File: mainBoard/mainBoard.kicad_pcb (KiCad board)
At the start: 4 copper layers, 132 x 85 mm, 78 parts, among them IC1 TCAN3414DR, J1 XT60PW-M, J10 RJ45, J11 RJ45, J12 Conn_01x03, J13 RJ45, J14 RJ45, J15 RJ45, J16 BM04B-SRSS-TB, J17 BM04B-SRSS-TB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

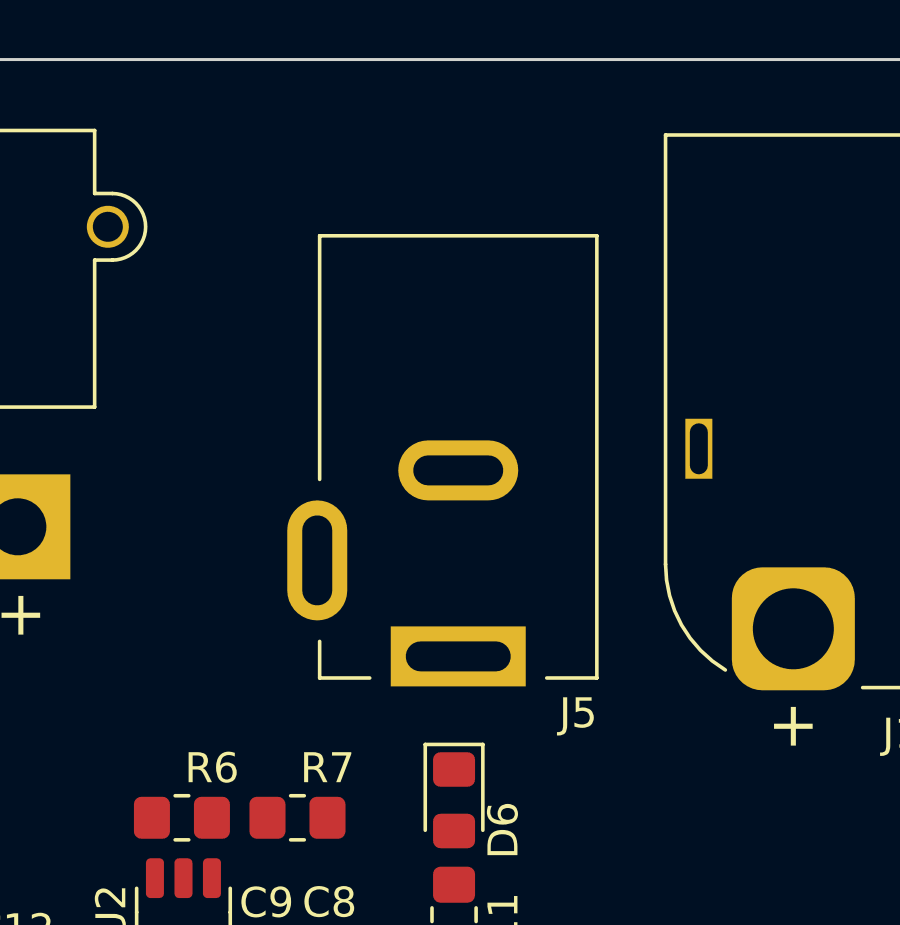
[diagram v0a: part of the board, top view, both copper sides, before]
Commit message: Moved barrel jack forward a bit
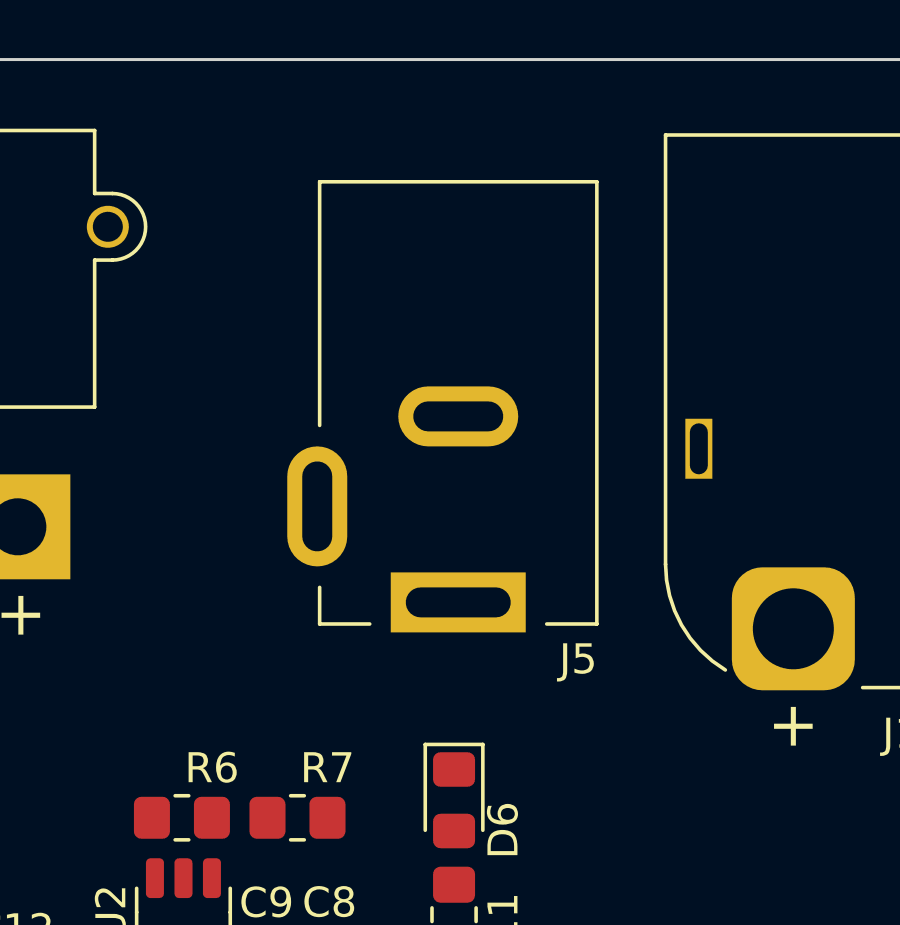
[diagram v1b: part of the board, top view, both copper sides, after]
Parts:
- moved J5 1.80 mm to (72.9, 30.1)
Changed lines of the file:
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@@
 	(footprint "Connector_BarrelJack:BarrelJack_Kycon_KLDX-0202-xC_Horizontal"
 		(layer "F.Cu")
-		(at 72.875 31.895 -90)
+		(at 72.875 30.095 -90)
 		(descr "DC Barrel Jack 2mm or 2.5mm center pin, https://www.kycon.com/Pub_Eng_Draw/KLDX-0202-AC%20&%20BC.pdf")
 		(tags "power jack 2mm 2.5mm KLDX-0202-BC KLDX-0202-AC")

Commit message: layed out mainboard as tano reccomended, added mounting holes, images, and new step file
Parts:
- removed D4, D5: 1SMA5925BT3G, Diode_SMD:D_SMA_Handsoldering
- removed D6, D7: LED, Diode_SMD:D_0805_2012Metric_Pad1.15x1.40mm_HandSolder
- removed R11, R12: 500, Resistor_SMD:R_0805_2012Metric_Pad1.20x1.40mm_HandSolder
- added H1: M4, MountingHole:MountingHole_4.3mm_M4_DIN965, F.Cu at (162.0, 19.0)
- added H2: M4, MountingHole:MountingHole_4.3mm_M4_DIN965, F.Cu at (264.0, 19.0)
- added H3: M4, MountingHole:MountingHole_4.3mm_M4_DIN965, F.Cu at (162.0, 86.0)
- added H4: M4, MountingHole:MountingHole_4.3mm_M4_DIN965, F.Cu at (264.0, 86.0)
- C10, C11, C12, C13, C8, C9, L2, Q2, R10, R14, R6, R7, U2: moved to B.Cu
- moved D3 211.1 mm to (258.3, 19.3), turned to 90 degrees
- moved R8 209.1 mm to (256.2, 19.3)
- moved J4 177.5 mm to (235.7, 28.6)
- moved C13 173.0 mm to (231.8, 41.0), turned to 180 degrees
- moved C12 173.0 mm to (231.8, 43.0), turned to 180 degrees
- moved L2 169.1 mm to (229.8, 47.6), turned to 0 degrees
- moved C11 165.0 mm to (227.7, 43.0), turned to 180 degrees
- moved R6 163.0 mm to (226.7, 36.7), turned to 0 degrees
- moved U2 162.9 mm to (226.6, 39.8)
- moved C9 157.3 mm to (223.8, 42.0)
- moved R7 155.3 mm to (222.8, 36.7), turned to 0 degrees
- moved C8 153.1 mm to (221.7, 42.0)
- moved C10 148.9 mm to (219.6, 42.0)
- moved Q2 144.7 mm to (214.8, 46.0), turned to -90 degrees
- moved R10 142.4 mm to (210.2, 48.3), turned to -90 degrees
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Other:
- board size 132 x 85 mm -> 110 x 75 mm

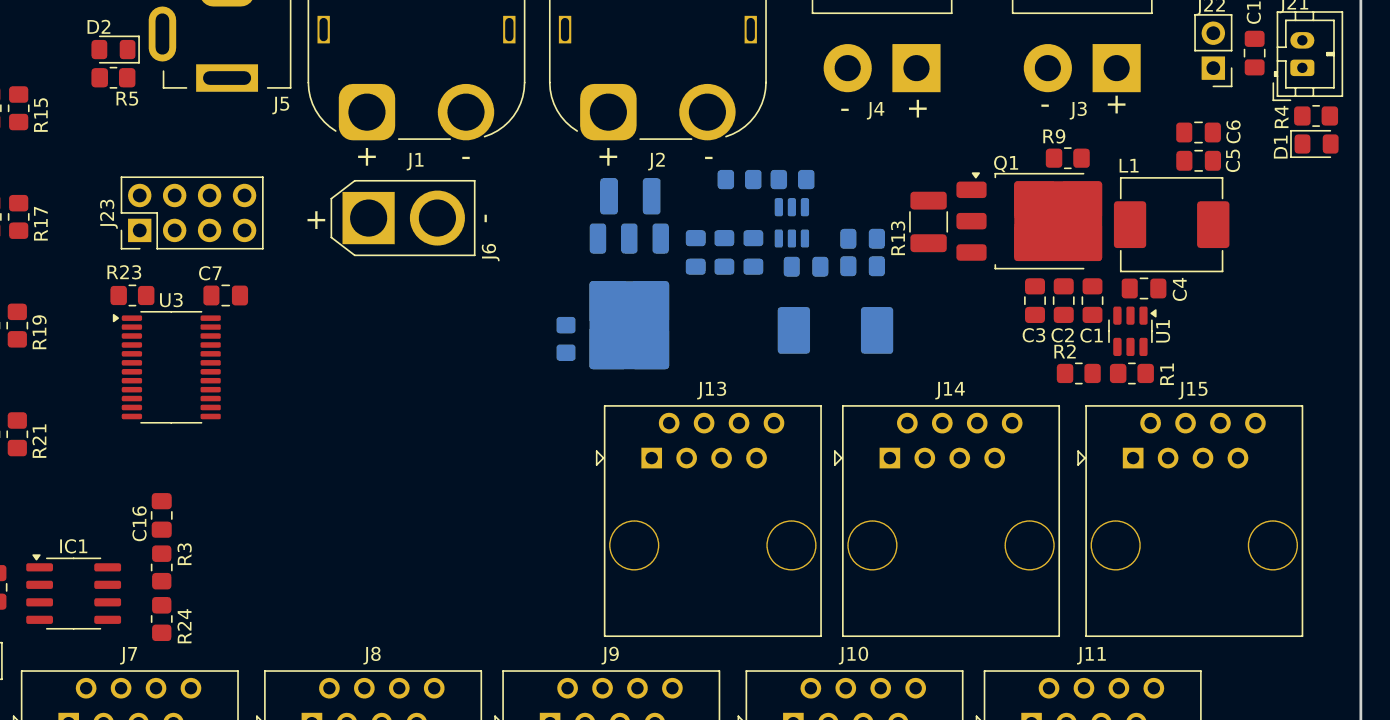
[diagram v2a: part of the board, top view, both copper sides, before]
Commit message: removed 3 of the can ports, re-layed out the buck converters, exported new step
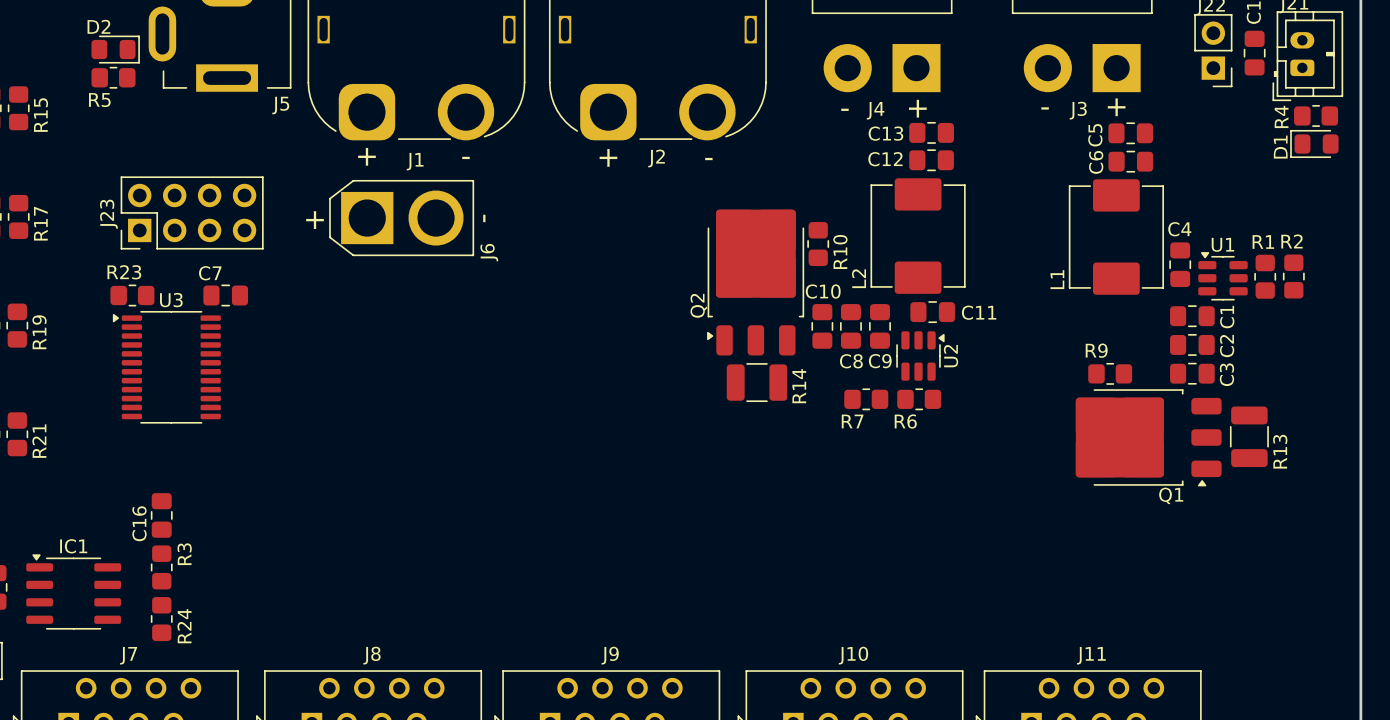
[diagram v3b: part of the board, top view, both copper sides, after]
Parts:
- removed J13, J14, J15: RJ45, Connector_RJ:RJ45_OST_PJ012-8P8CX_Vertical
- C10, C11, C12, C13, C8, C9, L2, Q2, R10, R14, R6, R7, U2: moved to F.Cu
- moved R13 28.1 mm to (259.9, 55.4), turned to -90 degrees
- moved R10 19.6 mm to (228.6, 41.4)
- moved R6 18.4 mm to (235.9, 52.7)
- moved R7 18.4 mm to (232.0, 52.7)
- moved Q1 17.2 mm to (251.7, 55.4), turned to 180 degrees
- moved R2 17.1 mm to (263.1, 43.7), turned to -90 degrees
- moved R14 16.4 mm to (224.1, 51.4)
- moved R9 16.0 mm to (249.8, 50.8), turned to 0 degrees
- moved U2 13.4 mm to (235.8, 49.5), turned to -90 degrees
- moved C3 12.6 mm to (255.8, 50.8), turned to 180 degrees
- moved R1 12.0 mm to (261.0, 43.7), turned to 90 degrees
- moved C8 10.7 mm to (230.9, 47.4), turned to 90 degrees
- moved C10 10.7 mm to (228.9, 47.4), turned to 90 degrees
- moved C9 10.7 mm to (233.0, 47.4), turned to 90 degrees
- moved C2 9.89 mm to (255.8, 48.7), turned to 180 degrees
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
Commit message: added a .wrl of the mainboard
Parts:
- moved C1 142.6 mm to (113.3, 51.4)
- moved C10 142.6 mm to (86.4, 52.2)
- moved C11 142.6 mm to (94.4, 51.1)
- moved C12 142.6 mm to (94.3, 40.1)
- moved C13 142.6 mm to (94.3, 38.1)
- moved C14 142.6 mm to (26.3, 71.1)
- moved C15 142.6 mm to (117.8, 32.3)
- moved C16 142.6 mm to (38.3, 65.9)
- moved C2 142.6 mm to (113.3, 53.5)
- moved C3 142.6 mm to (113.3, 55.6)
- moved C4 142.6 mm to (112.4, 47.7)
- moved C5 142.6 mm to (108.8, 38.1)
- moved C6 142.6 mm to (108.8, 40.2)
- moved C7 142.6 mm to (43.0, 49.9)
- moved C8 142.6 mm to (88.4, 52.2)
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
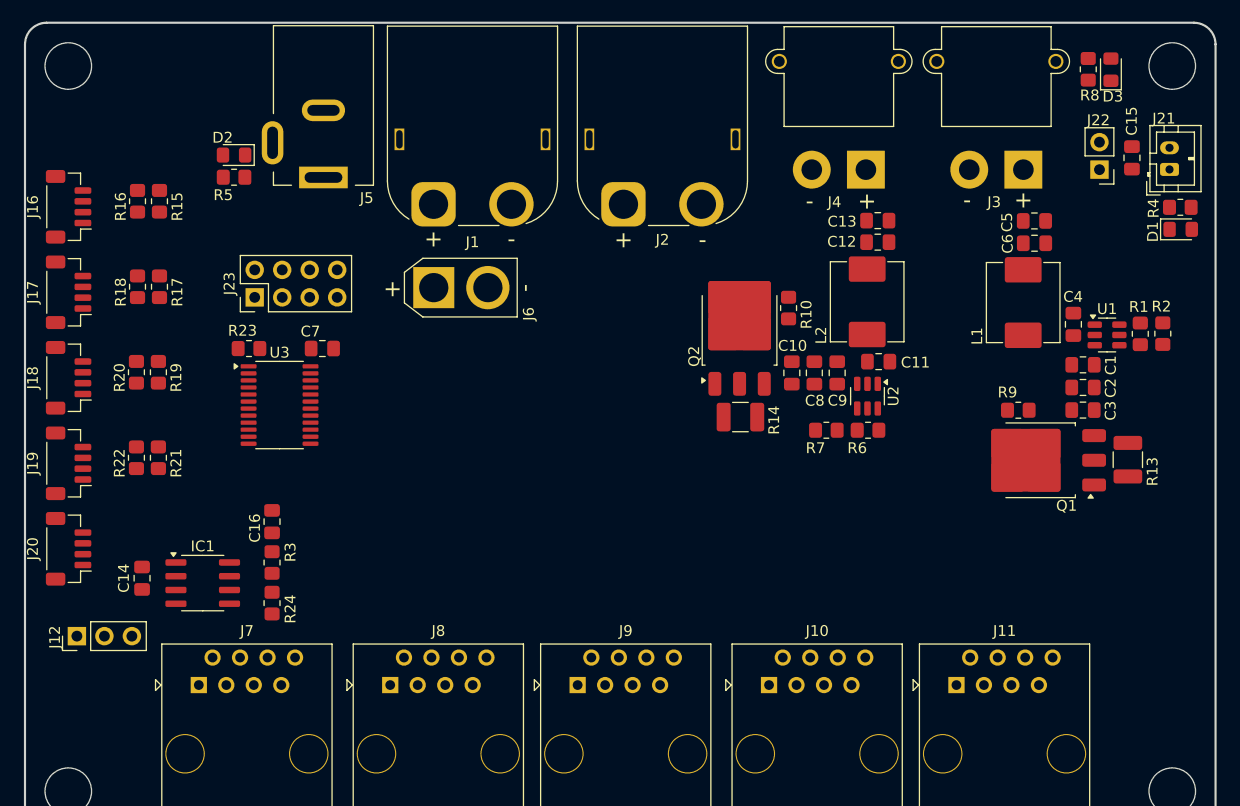
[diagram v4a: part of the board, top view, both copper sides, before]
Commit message: added labels, moved a few items
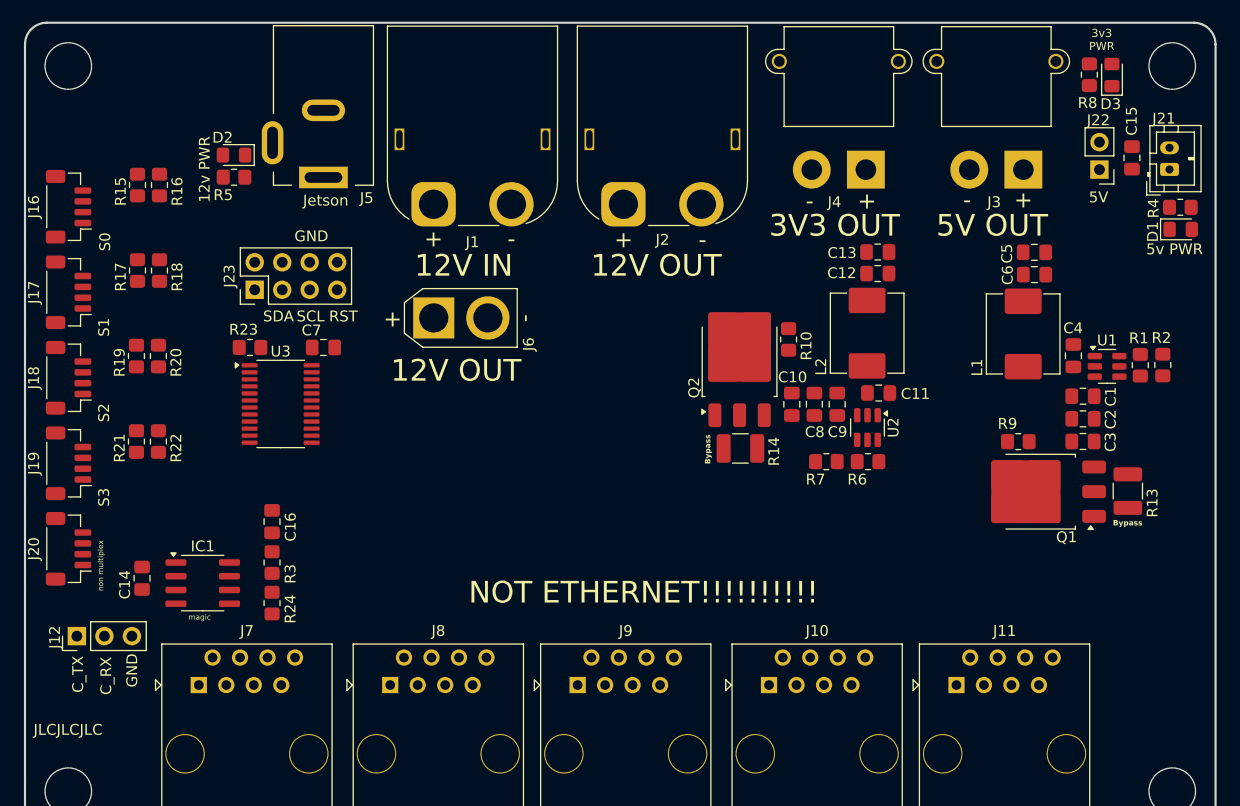
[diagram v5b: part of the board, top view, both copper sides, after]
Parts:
- added G***: LOGO, LOGO, B.Cu at (105.9, 55.2)
- moved C2 2.90 mm to (113.3, 56.4)
- moved C4 2.90 mm to (112.4, 50.6)
- moved C6 2.90 mm to (108.8, 43.1)
- moved Q2 2.90 mm to (81.5, 51.0)
- moved R14 2.90 mm to (81.6, 59.1)
- moved R6 2.90 mm to (93.4, 60.4)
- moved R7 2.90 mm to (89.5, 60.4)
- moved C1 2.90 mm to (113.3, 54.3)
- moved C10 2.90 mm to (86.4, 55.1)
- moved C11 2.90 mm to (94.4, 54.0)
- moved C12 2.90 mm to (94.3, 43.0)
- moved C13 2.90 mm to (94.3, 41.0)
- moved C3 2.90 mm to (113.3, 58.5)
- moved C5 2.90 mm to (108.8, 41.0)
- moved C8 2.90 mm to (88.4, 55.1)
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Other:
- board text added: "12V IN"
- board text added: "12V OUT"
- board text added: "12v PWR"
- board text added: "3V3 OUT"
- board text added: "3v3 PWR"
- board text added: "5V"
- board text added: "5V OUT"
- board text added: "5v PWR"
- board text added: "Bypass"
- board text added: "C_RX"
- board text added: "C_TX"
- board text added: "GND"
- board text added: "JLCJLCJLC"
- board text added: "Jetson"
- board text added: "Main Board"
- board text added: "NOT ETHERNET!!!!!!!!!!"
- board text added: "RST"
- board text added: "S0"
- board text added: "S1"
- board text added: "S2"
- board text added: "S3"
- board text added: "SCL"
- board text added: "SDA"
- board text added: "SP (BigPierogi)"
- board text added: "V2"
- board text added: "magic"
- board text added: "non multiplex"

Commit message: Routed board, created gerbers
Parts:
- moved C16 0.40 mm to (38.7, 65.9)
- moved R24 0.40 mm to (38.7, 73.4)
- moved R3 0.40 mm to (38.7, 69.7)
- moved R16 0.30 mm to (28.2, 34.8)
- moved R18 0.30 mm to (28.2, 42.7)
- moved R20 0.30 mm to (28.1, 50.6)
- moved R22 0.30 mm to (28.1, 58.5)
- moved J6 0.30 mm to (53.3, 46.8)
- moved J16 0.20 mm to (19.7, 36.8)
- moved J17 0.20 mm to (19.7, 44.7)
- moved J18 0.20 mm to (19.7, 52.6)
- moved J19 0.20 mm to (19.7, 60.5)
- moved J20 0.20 mm to (19.7, 68.4)
- moved L1 0.10 mm to (107.6, 48.6)
- moved C4 0.10 mm to (112.3, 50.6)
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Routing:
- net +3V3: track 0.00 -> 271.7 mm, vias 0 -> 8
- net CANP: track 0.00 -> 145.5 mm, vias 0 -> 2
- net CANN: track 0.00 -> 140.2 mm, vias 0 -> 6
- net SCL1: track 0.00 -> 57.9 mm, vias 0 -> 2
- net SDA1: track 0.00 -> 54.6 mm, vias 0 -> 3
- net SCLS0: track 0.00 -> 34.3 mm
- net SDAS0: track 0.00 -> 33.2 mm, vias 0 -> 2
- net +5V: track 0.00 -> 31.9 mm, vias 0 -> 7
- net GND: track 0.00 -> 29.1 mm, vias 0 -> 202
- net SCLS1: track 0.00 -> 26.9 mm
- net SDAS1: track 0.00 -> 26.9 mm, vias 0 -> 2
- net GPIO_GCLK: track 0.00 -> 25.5 mm
- net SCLS3: track 0.00 -> 21.5 mm
- net SCLS2: track 0.00 -> 20.6 mm
- net SDAS2: track 0.00 -> 19.2 mm, vias 0 -> 2
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- added copper zone on F.Cu, net +12V
- added copper zone on F.Cu, net +3V3
- added copper zone on F.Cu, net +5V
- added copper zone on B.Cu, net GND
- added copper zone on F.Cu, net GND
- added copper zone on In1.Cu, net GND
- added copper zone on In2.Cu, net GND
- added copper zone on F.Cu, net Net-(Q1-S)
- added copper zone on F.Cu, net Net-(Q2-S)
- added copper zone on F.Cu, net Net-(U1-SW)
- added copper zone on F.Cu, net Net-(U2-SW)
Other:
- board text added: "+"
- board text added: "-"
- board text added: "5A"
- board text added: "JLCJLCJLCJLC"
- board text added: "NOT ETHERNET!!!!!!!!!!!!!!!!!!!!!!!!!!!!!"
- board text removed: "JLCJLCJLC"
- board text removed: "NOT ETHERNET!!!!!!!!!!"
